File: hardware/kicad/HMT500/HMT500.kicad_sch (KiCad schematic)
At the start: 0 parts

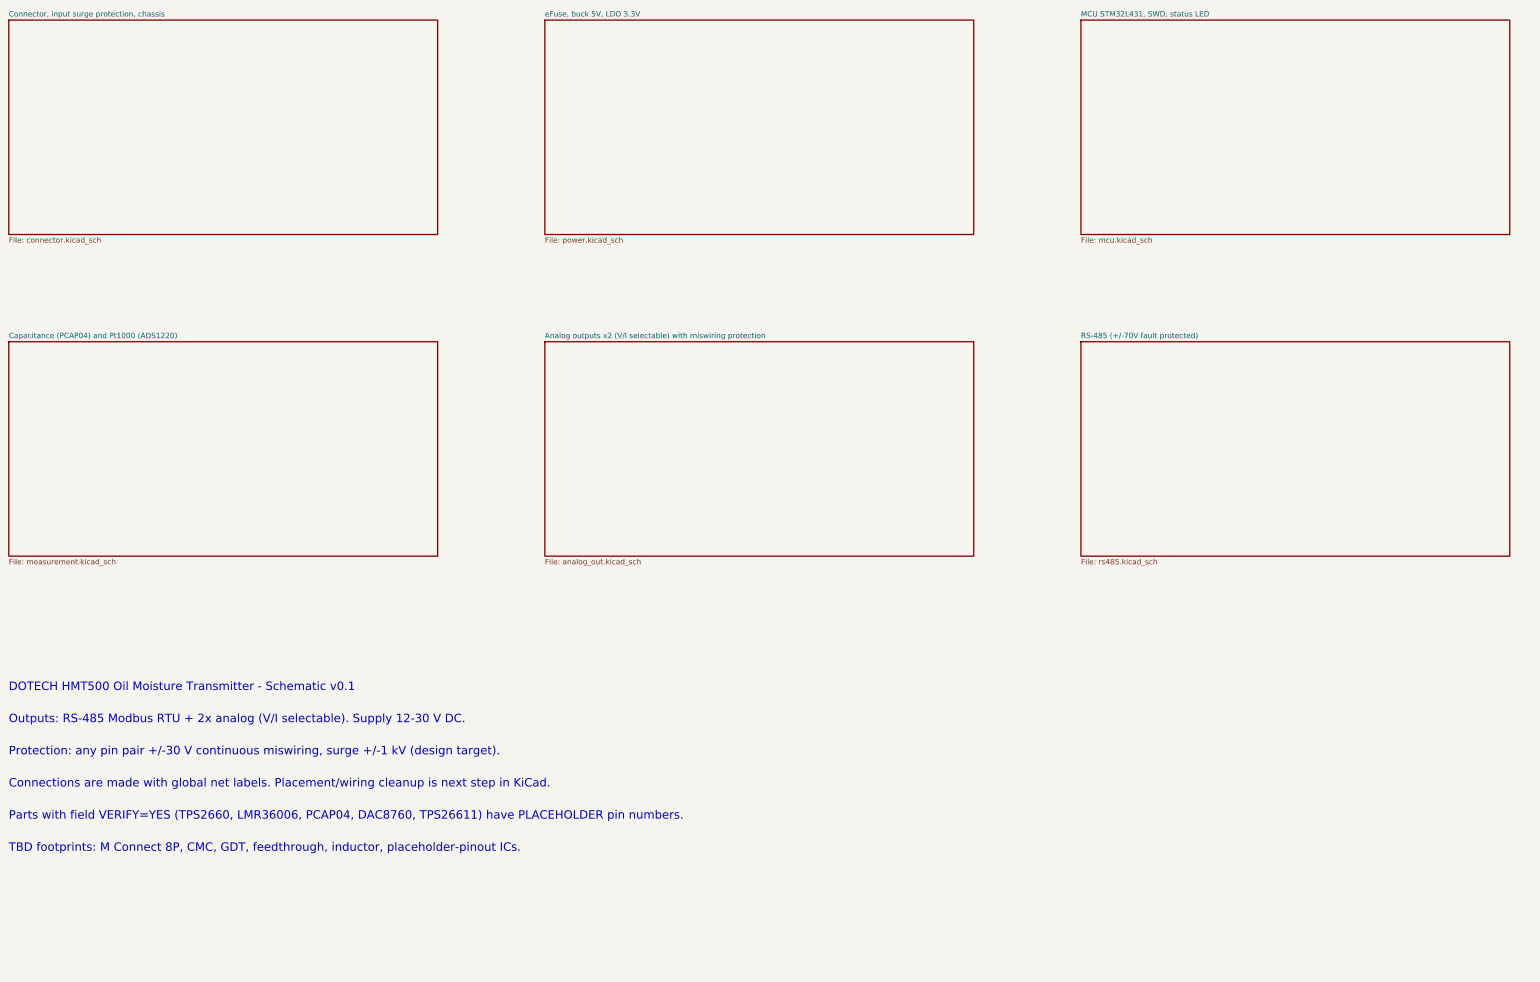
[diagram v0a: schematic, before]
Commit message: KiCad schematic v0.2: hand-laid-out, wired, readable sheets with power symbols and functional blocks
Replaces the label-only v0.1. Drawing rules are validated at generation and
the drawn netlist is checked against design intent (71 nets, 0 errors).

Co-Authored-By: Claude Opus 5.5 <noreply@anthropic.com>
Claude-Session: https://claude.ai/code/session_01JA2o8uJsqp9Vzsg4b665ev
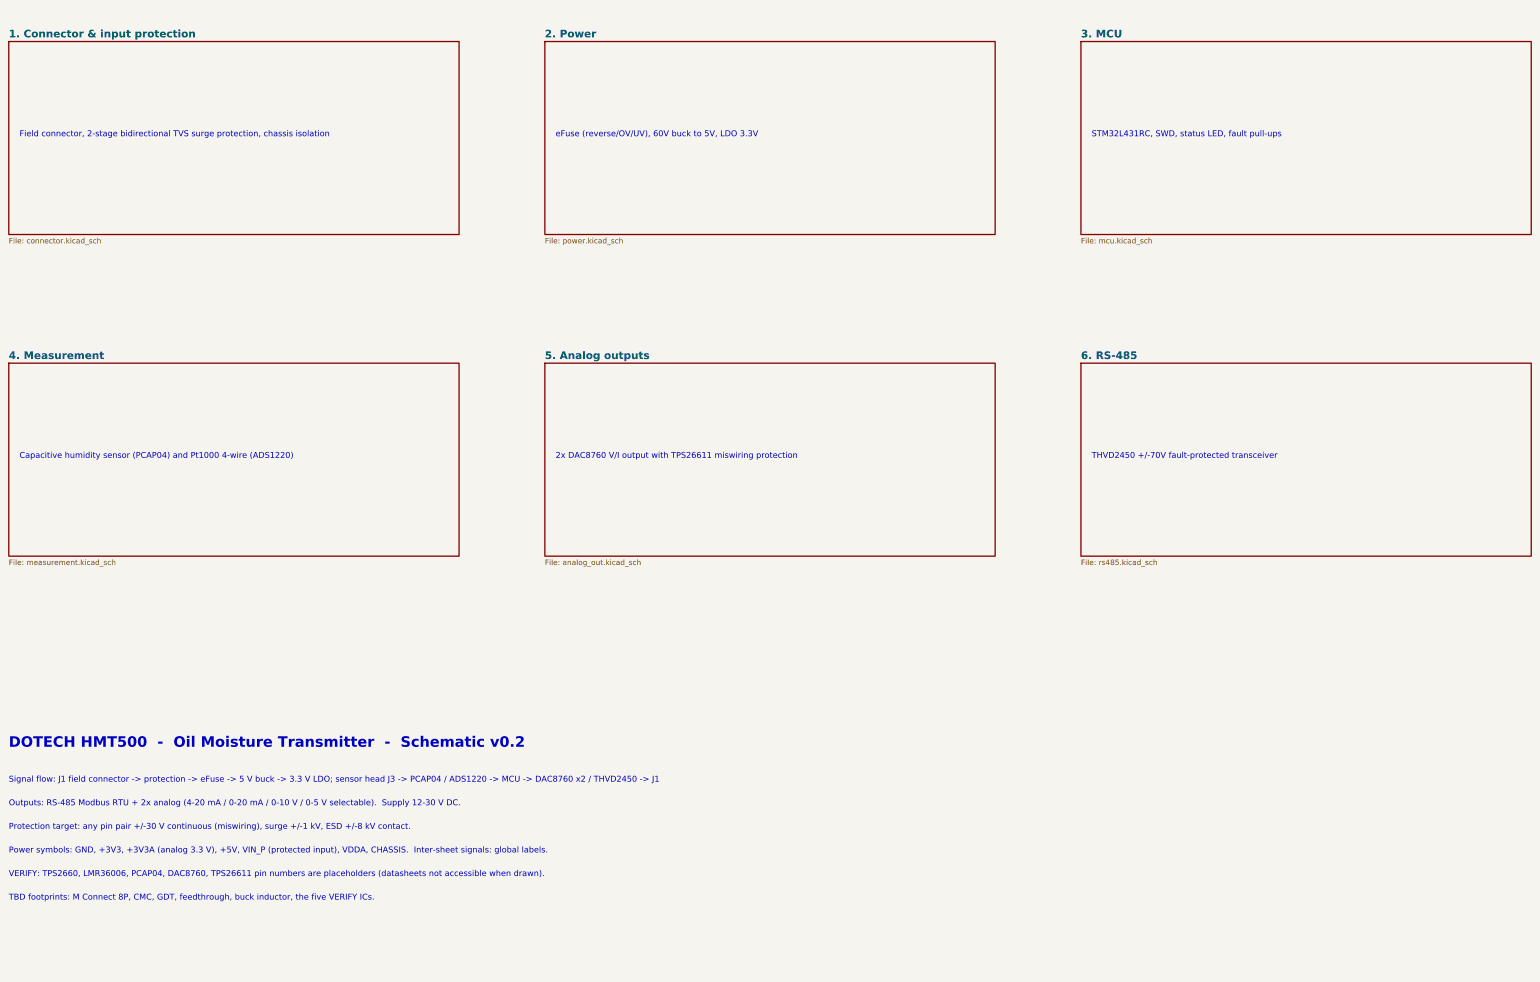
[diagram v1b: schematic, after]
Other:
- sheet Analog outputs x2 (V/I selectable) with miswiring protection renamed 5. Analog outputs
- sheet Capacitance (PCAP04) and Pt1000 (ADS1220) renamed 4. Measurement
- sheet Connector, input surge protection, chassis renamed 1. Connector & input protection
- sheet MCU STM32L431, SWD, status LED renamed 3. MCU
- sheet RS-485 (+/-70V fault protected) renamed 6. RS-485
- sheet eFuse, buck 5V, LDO 3.3V renamed 2. Power
- note added: "2x DAC8760 V/I output with TPS26611 miswiring protection"
- note added: "Capacitive humidity sensor (PCAP04) and Pt1000 4-wire (ADS1220)"
- note added: "DOTECH HMT500 - Oil Moisture Transmitter - Schematic v0.2"
- note added: "Field connector, 2-stage bidirectional TVS surge protection, chassis isolation"
- note added: "Outputs: RS-485 Modbus RTU + 2x analog (4-20 mA / 0-20 mA / 0-10 V / 0-5 V selectable). Supply 12-30 V DC."
- note added: "Power symbols: GND, +3V3, +3V3A (analog 3.3 V), +5V, VIN_P (protected input), VDDA, CHASSIS. Inter-sheet signals: global labels."
- note added: "Protection target: any pin pair +/-30 V continuous (miswiring), surge +/-1 kV, ESD +/-8 kV contact."
- note added: "STM32L431RC, SWD, status LED, fault pull-ups"
- note added: "Signal flow: J1 field connector -> protection -> eFuse -> 5 V buck -> 3.3 V LDO; sensor head J3 -> PCAP04 / ADS1220 -> MCU -> DAC8760 x2 / THVD2450 -> J1"
- note added: "TBD footprints: M Connect 8P, CMC, GDT, feedthrough, buck inductor, the five VERIFY ICs."
- note added: "THVD2450 +/-70V fault-protected transceiver"
- note added: "VERIFY: TPS2660, LMR36006, PCAP04, DAC8760, TPS26611 pin numbers are placeholders (datasheets not accessible when drawn)."
- note added: "eFuse (reverse/OV/UV), 60V buck to 5V, LDO 3.3V"
- note removed: "Connections are made with global net labels. Placement/wiring cleanup is next step in KiCad."
- note removed: "DOTECH HMT500 Oil Moisture Transmitter - Schematic v0.1"
- note removed: "Outputs: RS-485 Modbus RTU + 2x analog (V/I selectable). Supply 12-30 V DC."
- note removed: "Parts with field VERIFY=YES (TPS2660, LMR36006, PCAP04, DAC8760, TPS26611) have PLACEHOLDER pin numbers."
- note removed: "Protection: any pin pair +/-30 V continuous miswiring, surge +/-1 kV (design target)."
- note removed: "TBD footprints: M Connect 8P, CMC, GDT, feedthrough, inductor, placeholder-pinout ICs."
- title: HMT500 - Top -> HMT500  Top
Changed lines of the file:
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@@
 (kicad_sch (version 20230121) (generator eeschema) (paper "A3")
-(title_block (title "HMT500 - Top") (date "2026-09-26") (rev "0.1") (company "DOTECH Co., Ltd.") (comment 1 "Oil moisture transmitter HMT500") (comment 2 "Generated by hardware/kicad/gen_hmt500.py - see docs/hw/circuit-design.md") (comment 3 "Symbols with VERIFY=YES have placeholder pin numbers"))
-(sheet (at 30.48 50.8) (size 101.6 50.8) (fields_autoplaced) (stroke (width 0.1524) (type solid)) (fill (color 0 0 0 0.0000)) (property "Sheetname" "Connector, input surge protection, chassis" (at 30.48 50.1 0) (effects (font (size 1.27 1.27)) (justify left bottom))) (property "Sheetfile" "connector.kicad_sch" (at 30.48 102.2 0) (effects (font (size 1.27 1.27)) (justify left top))) (instances (project "HMT500" (path "/1ebb025b-11bd-5f7c-aaab-41e2a750e8b3" (page "2")))))
-(sheet (at 157.48 50.8) (size 101.6 50.8) (fields_autoplaced) (stroke (width 0.1524) (type solid)) (fill (color 0 0 0 0.0000)) (property "Sheetname" "eFuse, buck 5V, LDO 3.3V" (at 157.48 50.1 0) (effects (font (size 1.27 1.27)) (justify left bottom))) (property "Sheetfile" "power.kicad_sch" (at 157.48 102.2 0) (effects (font (size 1.27 1.27)) (justify left top))) (instances (project "HMT500" (path "/1ebb025b-11bd-5f7c-aaab-41e2a750e8b3" (page "3")))))
-(sheet (at 284.48 50.8) (size 101.6 50.8) (fields_autoplaced) (stroke (width 0.1524) (type solid)) (fill (color 0 0 0 0.0000)) (property "Sheetname" "MCU STM32L431, SWD, status LED" (at 284.48 50.1 0) (effects (font (size 1.27 1.27)) (justify left bottom))) (property "Sheetfile" "mcu.kicad_sch" (at 284.48 102.2 0) (effects (font (size 1.27 1.27)) (justify left top))) (instances (project "HMT500" (path "/1ebb025b-11bd-5f7c-aaab-41e2a750e8b3" (page "4")))))
-(sheet (at 30.48 127) (size 101.6 50.8) (fields_autoplaced) (stroke (width 0.1524) (type solid)) (fill (color 0 0 0 0.0000)) (property "Sheetname" "Capacitance (PCAP04) and Pt1000 (ADS1220)" (at 30.48 126.3 0) (effects (font (size 1.27 1.27)) (justify left bottom))) (property "Sheetfile" "measurement.kicad_sch" (at 30.48 178.4 0) (effects (font (size 1.27 1.27)) (justify left top))) (instances (project "HMT500" (path "/1ebb025b-11bd-5f7c-aaab-41e2a750e8b3" (page "5")))))
-(sheet (at 157.48 127) (size 101.6 50.8) (fields_autoplaced) (stroke (width 0.1524) (type solid)) (fill (color 0 0 0 0.0000)) (property "Sheetname" "Analog outputs x2 (V/I selectable) with miswiring protection" (at 157.48 126.3 0) (effects (font (size 1.27 1.27)) (justify left bottom))) (property "Sheetfile" "analog_out.kicad_sch" (at 157.48 178.4 0) (effects (font (size 1.27 1.27)) (justify left top))) (instances (project "HMT500" (path "/1ebb025b-11bd-5f7c-aaab-41e2a750e8b3" (page "6")))))
-(sheet (at 284.48 127) (size 101.6 50.8) (fields_autoplaced) (stroke (width 0.1524) (type solid)) (fill (color 0 0 0 0.0000)) (property "Sheetname" "RS-485 (+/-70V fault protected)" (at 284.48 126.3 0) (effects (font (size 1.27 1.27)) (justify left bottom))) (property "Sheetfile" "rs485.kicad_sch" (at 284.48 178.4 0) (effects (font (size 1.27 1.27)) (justify left top))) (instances (project "HMT500" (path "/1ebb025b-11bd-5f7c-aaab-41e2a750e8b3" (page "7")))))
-(text "DOTECH HMT500 Oil Moisture Transmitter - Schematic v0.1" (at 30.48 210 0) (effects (font (size 2 2)) (justify left bottom)))
-(text "Outputs: RS-485 Modbus RTU + 2x analog (V/I selectable). Supply 12-30 V DC." (at 30.48 217.62 0) (effects (font (size 2 2)) (justify left bottom)))
-(text "Protection: any pin pair +/-30 V continuous miswiring, surge +/-1 kV (design target)." (at 30.48 225.24 0) (effects (font (size 2 2)) (justify left bottom)))
-(text "Connections are made with global net labels. Placement/wiring cleanup is next step in KiCad." (at 30.48 232.86 0) (effects (font (size 2 2)) (justify left bottom)))
-(text "Parts with field VERIFY=YES (TPS2660, LMR36006, PCAP04, DAC8760, TPS26611) have PLACEHOLDER pin numbers." (at 30.48 240.48 0) (effects (font (size 2 2)) (justify left bottom)))
-(text "TBD footprints: M Connect 8P, CMC, GDT, feedthrough, inductor, placeholder-pinout ICs." (at 30.48 248.1 0) (effects (font (size 2 2)) (justify left bottom)))
+(title_block (title "HMT500  Top") (date "2026-09-26") (rev "0.2") (company "DOTECH Co., Ltd.") (comment 1 "Oil moisture transmitter HMT500 - RS-485 + 2x V/I analog output") (comment 2 "Design notes: docs/hw/circuit-design.md") (comment 3 "VERIFY=YES parts: placeholder pin numbers (TPS2660, LMR36006, PCAP04, DAC8760, TPS26611)"))
+(sheet (at 30.48 55.88) (size 106.68 45.72) (fields_autoplaced) (stroke (width 0.1524) (type solid)) (fill (color 0 0 0 0.0000)) (property "Sheetname" "1. Connector & input protection" (at 30.48 55.118 0) (effects (font (size 1.8 1.8) bold) (justify left bottom))) (property "Sheetfile" "connector.kicad_sch" (at 30.48 102.362 0) (effects (font (size 1.27 1.27)) (justify left top))) (instances (project "HMT500" (path "/1ebb025b-11bd-5f7c-aaab-41e2a750e8b3" (page "2")))))
+(text "Field connector, 2-stage bidirectional TVS surge protection, chassis isolation" (at 33.02 78.74 0) (effects (font (size 1.4 1.4)) (justify left bottom)))
+(sheet (at 157.48 55.88) (size 106.68 45.72) (fields_autoplaced) (stroke (width 0.1524) (type solid)) (fill (color 0 0 0 0.0000)) (property "Sheetname" "2. Power" (at 157.48 55.118 0) (effects (font (size 1.8 1.8) bold) (justify left bottom))) (property "Sheetfile" "power.kicad_sch" (at 157.48 102.362 0) (effects (font (size 1.27 1.27)) (justify left top))) (instances (project "HMT500" (path "/1ebb025b-11bd-5f7c-aaab-41e2a750e8b3" (page "3")))))
+(text "eFuse (reverse/OV/UV), 60V buck to 5V, LDO 3.3V" (at 160.02 78.74 0) (effects (font (size 1.4 1.4)) (justify left bottom)))
+(sheet (at 284.48 55.88) (size 106.68 45.72) (fields_autoplaced) (stroke (width 0.1524) (type solid)) (fill (color 0 0 0 0.0000)) (property "Sheetname" "3. MCU" (at 284.48 55.118 0) (effects (font (size 1.8 1.8) bold) (justify left bottom))) (property "Sheetfile" "mcu.kicad_sch" (at 284.48 102.362 0) (effects (font (size 1.27 1.27)) (justify left top))) (instances (project "HMT500" (path "/1ebb025b-11bd-5f7c-aaab-41e2a750e8b3" (page "4")))))
+(text "STM32L431RC, SWD, status LED, fault pull-ups" (at 287.02 78.74 0) (effects (font (size 1.4 1.4)) (justify left bottom)))
+(sheet (at 30.48 132.08) (size 106.68 45.72) (fields_autoplaced) (stroke (width 0.1524) (type solid)) (fill (color 0 0 0 0.0000)) (property "Sheetname" "4. Measurement" (at 30.48 131.318 0) (effects (font (size 1.8 1.8) bold) (justify left bottom))) (property "Sheetfile" "measurement.kicad_sch" (at 30.48 178.562 0) (effects (font (size 1.27 1.27)) (justify left top))) (instances (project "HMT500" (path "/1ebb025b-11bd-5f7c-aaab-41e2a750e8b3" (page "5")))))
+(text "Capacitive humidity sensor (PCAP04) and Pt1000 4-wire (ADS1220)" (at 33.02 154.94 0) (effects (font (size 1.4 1.4)) (justify left bottom)))
+(sheet (at 157.48 132.08) (size 106.68 45.72) (fields_autoplaced) (stroke (width 0.1524) (type solid)) (fill (color 0 0 0 0.0000)) (property "Sheetname" "5. Analog outputs" (at 157.48 131.318 0) (effects (font (size 1.8 1.8) bold) (justify left bottom))) (property "Sheetfile" "analog_out.kicad_sch" (at 157.48 178.562 0) (effects (font (size 1.27 1.27)) (justify left top))) (instances (project "HMT500" (path "/1ebb025b-11bd-5f7c-aaab-41e2a750e8b3" (page "6")))))
+(text "2x DAC8760 V/I output with TPS26611 miswiring protection" (at 160.02 154.94 0) (effects (font (size 1.4 1.4)) (justify left bottom)))
+(sheet (at 284.48 132.08) (size 106.68 45.72) (fields_autoplaced) (stroke (width 0.1524) (type solid)) (fill (color 0 0 0 0.0000)) (property "Sheetname" "6. RS-485" (at 284.48 131.318 0) (effects (font (size 1.8 1.8) bold) (justify left bottom))) (property "Sheetfile" "rs485.kicad_sch" (at 284.48 178.562 0) (effects (font (size 1.27 1.27)) (justify left top))) (instances (project "HMT500" (path "/1ebb025b-11bd-5f7c-aaab-41e2a750e8b3" (page "7")))))
+(text "THVD2450 +/-70V fault-protected transceiver" (at 287.02 154.94 0) (effects (font (size 1.4 1.4)) (justify left bottom)))
+(text "DOTECH HMT500  -  Oil Moisture Transmitter  -  Schematic v0.2" (at 30.48 223.52 0) (effects (font (size 2.5 2.5) bold) (justify left bottom)))
+(text "Signal flow: J1 field connector -> protection -> eFuse -> 5 V buck -> 3.3 V LDO; sensor head J3 -> PCAP04 / ADS1220 -> MCU -> DAC8760 x2 / THVD2450 -> J1" (at 30.48 231.648 0) (effects (font (size 1.4 1.4)) (justify left bottom)))
+(text "Outputs: RS-485 Modbus RTU + 2x analog (4-20 mA / 0-20 mA / 0-10 V / 0-5 V selectable).  Supply 12-30 V DC." (at 30.48 237.236 0) (effects (font (size 1.4 1.4)) (justify left bottom)))
+(text "Protection target: any pin pair +/-30 V continuous (miswiring), surge +/-1 kV, ESD +/-8 kV contact." (at 30.48 242.824 0) (effects (font (size 1.4 1.4)) (justify left bottom)))
+(text "Power symbols: GND, +3V3, +3V3A (analog 3.3 V), +5V, VIN_P (protected input), VDDA, CHASSIS.  Inter-sheet signals: global labels." (at 30.48 248.412 0) (effects (font (size 1.4 1.4)) (justify left bottom)))
+(text "VERIFY: TPS2660, LMR36006, PCAP04, DAC8760, TPS26611 pin numbers are placeholders (datasheets not accessible when drawn)." (at 30.48 254 0) (effects (font (size 1.4 1.4)) (justify left bottom)))
+(text "TBD footprints: M Connect 8P, CMC, GDT, feedthrough, buck inductor, the five VERIFY ICs." (at 30.48 259.588 0) (effects (font (size 1.4 1.4)) (justify left bottom)))
 (sheet_instances (path "/" (page "1")))
 )
